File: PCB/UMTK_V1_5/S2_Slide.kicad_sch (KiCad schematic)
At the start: 6 parts, among them J6 JST 4pin, J7 47589-0001, J8 10033526-N3212LF

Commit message: Updating Schematic
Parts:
- added U11, U12: SN74LVC1T45DCK, Package_TO_SOT_SMD:SOT-363_SC-70-6, symbol Logic_LevelTranslator:SN74LVC1T45DCK
- JP1: value Slide_DAT_Swap -> SLIDE_DAT_DIR
- JP2: value Slide_CLK_Swap -> SLIDE_CLK_DIR
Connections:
- net +5V: now also U11.6 (VCCB), U12.6 (VCCB)
- net GND: now also JP1.3 (B), JP2.1 (A), U11.2 (GND), U12.2 (GND)
- net SLIDE_CLK: now also U11.3 (A); no longer J6.3, J7.3 (D+), J8.3 (D+), JP1.3 (B), JP2.1 (A), JP2.2 (C)
- net SLIDE_DAT: now also U12.3 (A); no longer J6.2, J7.2 (D-), J8.2 (D-), JP1.1 (A), JP1.2 (C), JP2.3 (B)
- new net: JP2.2 (C), U12.5 (DIR)
- new net: JP1.2 (C), U11.5 (DIR)
- new net VDD: JP1.1 (A), JP2.3 (B), U11.1 (VCCA), U12.1 (VCCA)
- new net _SLIDE_CLK: J6.3, J7.3 (D+), J8.3 (D+), U11.4 (B), U12.4 (B)
- new net _SLIDE_DAT_: J6.2, J7.2 (D-), J8.2 (D-)
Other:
- moved on the sheet: J6, J7, J8, JP3

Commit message: Schematic Done, Assigning footprint
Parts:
- removed JP1: SLIDE_DAT_DIR, symbol Jumper:Jumper_3_Bridged12
- removed JP2: SLIDE_CLK_DIR, symbol Jumper:Jumper_3_Bridged12
- renumbered JP3 to JP2
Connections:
- net SLIDE_DAT_DIR: now reaches U12.5 (DIR)
- net SLIDE_CLK_DIR: now reaches U11.5 (DIR)

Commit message: Footprint assign
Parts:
- J6: footprint 4Pin JST -> Connector_JST:JST_XH_B2B-XH-AM_1x02_P2.50mm_Vertical
- J7: footprint MOLX-47589-0001_V -> digikey-footprints:USB_Micro_AB_Female_0475890001
- J8: footprint FCI-10033526-N3212LF_V -> digikey-footprints:USB_Mini_B_Female_548190519
- JP2: footprint (none) -> Jumper:SolderJumper-3_P1.3mm_Bridged12_Pad1.0x1.5mm
- U11, U12: footprint Package_TO_SOT_SMD:SOT-363_SC-70-6 -> Package_TO_SOT_SMD:SOT-23-6
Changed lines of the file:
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@@
 			)
 		)
-		(property "Footprint" "4Pin JST"
+		(property "Footprint" "Connector_JST:JST_XH_B2B-XH-AM_1x02_P2.50mm_Vertical"
 			(at 152.4 105.41 0)
 			(effects
@@
 			)
 		)
-		(property "Footprint" "FCI-10033526-N3212LF_V"
+		(property "Footprint" "digikey-footprints:USB_Mini_B_Female_548190519"
 			(at 210.82 88.9 0)
 			(effects
@@
 			)
 		)
-		(property "Footprint" ""
+		(property "Footprint" "Jumper:SolderJumper-3_P1.3mm_Bridged12_Pad1.0x1.5mm"
 			(at 118.11 91.44 0)
 			(effects
@@
 			)
 		)
-		(property "Footprint" "MOLX-47589-0001_V"
+		(property "Footprint" "digikey-footprints:USB_Micro_AB_Female_0475890001"
 			(at 175.26 88.9 0)
 			(effects
@@
 			)
 		)
-		(property "Footprint" "Package_TO_SOT_SMD:SOT-363_SC-70-6"
+		(property "Footprint" "Package_TO_SOT_SMD:SOT-23-6"
 			(at 64.77 95.25 0)
 			(effects
@@
 			)
 		)
-		(property "Footprint" "Package_TO_SOT_SMD:SOT-363_SC-70-6"
+		(property "Footprint" "Package_TO_SOT_SMD:SOT-23-6"
 			(at 64.77 140.97 0)
 			(effects

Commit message: ERC good, imported into PCB
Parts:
- J6: footprint Connector_JST:JST_XH_B2B-XH-AM_1x02_P2.50mm_Vertical -> Connector_JST:JST_XH_B4B-XH-A_1x04_P2.50mm_Vertical
- U11, U12: footprint Package_TO_SOT_SMD:SOT-23-6 -> Package_TO_SOT_SMD:SOT-363_SC-70-6
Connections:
- no-connect marks 0 -> 2
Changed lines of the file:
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@@
 		(color 0 0 0 0)
+	)
+	(no_connect
+		(at 205.74 99.06)
+	)
+	(no_connect
+		(at 170.18 99.06)
 	)
 	(wire
@@
 			)
 		)
-		(property "Description" ""
+		(property "Description" "Power symbol creates a global label with name \"+5V\""
 			(at 111.76 86.36 0)
 			(effects
@@
 			)
 		)
-		(property "Description" ""
+		(property "Description" "Power symbol creates a global label with name 'GND'"
 			(at 170.18 119.38 0)
 			(effects
@@
 			)
 		)
-		(property "Footprint" "Connector_JST:JST_XH_B2B-XH-AM_1x02_P2.50mm_Vertical"
+		(property "Footprint" "Connector_JST:JST_XH_B4B-XH-A_1x04_P2.50mm_Vertical"
 			(at 152.4 105.41 0)
 			(effects
@@
 			)
 		)
-		(property "Description" ""
+		(property "Description" "Mini USB B-Type, 5-Pin SMD, RoHS, Tape and Reel"
 			(at 210.82 88.9 0)
 			(effects
@@
 			)
 		)
-		(property "Description" ""
+		(property "Description" "Jumper, 3-pole, pins 1+2 closed/bridged"
 			(at 118.11 91.44 0)
 			(effects
@@
 			)
 		)
-		(property "Description" ""
+		(property "Description" "Right Angle Female Type AB Micro USB Connector, 30 V, 1.8 A, -30 to 85 degC, RoHS, Tape and Reel"
 			(at 175.26 88.9 0)
 			(effects
@@
 			)
 		)
-		(property "Description" ""
+		(property "Description" "Power symbol creates a global label with name 'GND'"
 			(at 144.78 115.57 0)
 			(effects
@@
 			)
 		)
-		(property "Description" ""
+		(property "Description" "Power symbol creates a global label with name \"+3V3\""
 			(at 109.22 97.79 0)
 			(effects
@@
 			)
 		)
-		(property "Footprint" "Package_TO_SOT_SMD:SOT-23-6"
+		(property "Footprint" "Package_TO_SOT_SMD:SOT-363_SC-70-6"
 			(at 64.77 95.25 0)
 			(effects
@@
 			)
 		)
-		(property "Footprint" "Package_TO_SOT_SMD:SOT-23-6"
+		(property "Footprint" "Package_TO_SOT_SMD:SOT-363_SC-70-6"
 			(at 64.77 140.97 0)
 			(effects
@@
 			)
 		)
-		(property "Description" ""
+		(property "Description" "Power symbol creates a global label with name 'GND'"
 			(at 205.74 119.38 0)
 			(effects

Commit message: Initial Place, Board Stack
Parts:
- removed J6: JST 4pin, Connector_JST:JST_XH_B4B-XH-A_1x04_P2.50mm_Vertical, symbol UMTK-altium-import:0_4Pin JST
- removed J7: 47589-0001, digikey-footprints:USB_Micro_AB_Female_0475890001, symbol UMTK-altium-import:0_USB-5-6SHLD
- added JP3: Slide Logic LVL, Jumper:SolderJumper-3_P1.3mm_Bridged12_Pad1.0x1.5mm, symbol Jumper:Jumper_3_Bridged12
- J8: footprint digikey-footprints:USB_Mini_B_Female_548190519 -> Connector_USB:USB_Mini-B_Wuerth_65100516121_Horizontal
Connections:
- net +3V3: now also JP3.1 (A)
- net +5V: now also JP3.3 (B); no longer U11.6 (VCCB), U12.6 (VCCB)
- net _SLIDE_DAT_: now also U12.4 (B)
- net _SLIDE_CLK renamed _SLIDE_CLK_
- net _SLIDE_CLK_: no longer U12.4 (B)
- new net _SLIDE_DATA_LVL_: JP3.2 (C), U11.6 (VCCB), U12.6 (VCCB)
- no-connect marks 2 -> 1
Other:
- moved on the sheet: J8

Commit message: Layout Started
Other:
- moved on the sheet: J8
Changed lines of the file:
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@@
 	(paper "A4")
 	(junction
-		(at 154.94 109.22)
+		(at 184.15 114.3)
 		(diameter 0)
 		(color 0 0 0 0)
 	)
 	(junction
-		(at 154.94 111.76)
+		(at 184.15 116.84)
 		(diameter 0)
 		(color 0 0 0 0)
 	)
 	(junction
-		(at 154.94 114.3)
+		(at 184.15 119.38)
 		(diameter 0)
 		(color 0 0 0 0)
 	)
 	(junction
-		(at 154.94 116.84)
+		(at 184.15 121.92)
 		(diameter 0)
 		(color 0 0 0 0)
 	)
 	(no_connect
-		(at 154.94 104.14)
+		(at 184.15 109.22)
 	)
 	(wire
@@
 	(wire
 		(pts
+			(xy 147.32 101.6) (xy 184.15 101.6)
+		)
+		(stroke
+			(width 0)
+			(type default)
+		)
+	)
+	(wire
+		(pts
 			(xy 107.95 121.92) (xy 110.49 121.92)
 		)
@@
 	(wire
 		(pts
-			(xy 154.94 124.46) (xy 154.94 116.84)
+			(xy 184.15 129.54) (xy 184.15 121.92)
 		)
 		(stroke
@@
 	(wire
 		(pts
-			(xy 154.94 114.3) (xy 154.94 111.76)
+			(xy 147.32 91.44) (xy 147.32 101.6)
+		)
+		(stroke
+			(width 0)
+			(type default)
+		)
+	)
+	(wire
+		(pts
+			(xy 184.15 119.38) (xy 184.15 116.84)
 		)
 		(stroke
@@
 	(wire
 		(pts
-			(xy 152.4 99.06) (xy 154.94 99.06)
+			(xy 181.61 104.14) (xy 184.15 104.14)
 		)
 		(stroke
@@
 	(wire
 		(pts
-			(xy 154.94 111.76) (xy 154.94 109.22)
+			(xy 184.15 116.84) (xy 184.15 114.3)
 		)
 		(stroke
@@
 	(wire
 		(pts
-			(xy 151.13 91.44) (xy 121.92 91.44)
-		)
-		(stroke
-			(width 0)
-			(type default)
-		)
-	)
-	(wire
-		(pts
 			(xy 110.49 121.92) (xy 110.49 120.65)
 		)
@@
 	(wire
 		(pts
-			(xy 151.13 96.52) (xy 151.13 91.44)
-		)
-		(stroke
-			(width 0)
-			(type default)
-		)
-	)
-	(wire
-		(pts
-			(xy 152.4 101.6) (xy 154.94 101.6)
-		)
-		(stroke
-			(width 0)
-			(type default)
-		)
-	)
-	(wire
-		(pts
-			(xy 151.13 96.52) (xy 154.94 96.52)
+			(xy 181.61 106.68) (xy 184.15 106.68)
+		)
+		(stroke
+			(width 0)
+			(type default)
+		)
+	)
+	(wire
+		(pts
+			(xy 121.92 91.44) (xy 147.32 91.44)
 		)
 		(stroke
@@
 	(wire
 		(pts
-			(xy 154.94 109.22) (xy 154.94 106.68)
+			(xy 184.15 114.3) (xy 184.15 111.76)
 		)
 		(stroke
@@
 	(wire
 		(pts
-			(xy 154.94 116.84) (xy 154.94 114.3)
+			(xy 184.15 121.92) (xy 184.15 119.38)
 		)
 		(stroke
@@
 	)
 	(label "_SLIDE_DAT_"
-		(at 152.4 99.06 180)
+		(at 181.61 104.14 180)
 		(fields_autoplaced yes)
 		(effects
@@
 	)
 	(label "_SLIDE_CLK_"
-		(at 152.4 101.6 180)
+		(at 181.61 106.68 180)
 		(fields_autoplaced yes)
 		(effects
@@
 	(symbol
 		(lib_id "UMTK-altium-import:0_USB-5-4SHLD")
-		(at 160.02 93.98 0)
+		(at 189.23 99.06 0)
 		(unit 1)
 		(exclude_from_sim no)
@@
 		(dnp no)
 		(property "Reference" "J8"
-			(at 159.766 93.726 0)
+			(at 188.976 98.806 0)
 			(effects
 				(font
@@
 		)
 		(property "Value" "10033526-N3212LF"
-			(at 159.766 122.174 0)
+			(at 188.976 127.254 0)
 			(effects
 				(font
@@
 		)
 		(property "Footprint" "Connector_USB:USB_Mini-B_Wuerth_65100516121_Horizontal"
-			(at 160.02 93.98 0)
+			(at 189.23 99.06 0)
 			(effects
 				(font
@@
 		)
 		(property "Datasheet" ""
-			(at 160.02 93.98 0)
+			(at 189.23 99.06 0)
 			(effects
 				(font
@@
 		)
 		(property "Description" "Mini USB B-Type, 5-Pin SMD, RoHS, Tape and Reel"
-			(at 160.02 93.98 0)
+			(at 189.23 99.06 0)
 			(effects
 				(font
@@
 		)
 		(property "PARTNUMBER" "10033526-N3212LF"
-			(at 154.432 90.17 0)
+			(at 183.642 95.25 0)
 			(effects
 				(font
@@
 		)
 		(property "DATASHEETVERSION" "Rev. N"
-			(at 154.432 90.17 0)
+			(at 183.642 95.25 0)
 			(effects
 				(font
@@
 		)
 		(property "TERMINATION STYLE" "Solder Pad"
-			(at 154.432 90.17 0)
+			(at 183.642 95.25 0)
 			(effects
 				(font
@@
 		)
 		(property "PACKAGING" "Reel"
-			(at 154.432 90.17 0)
+			(at 183.642 95.25 0)
 			(effects
 				(font
@@
 		)
 		(property "SHELL PLATING" "Nickel"
-			(at 154.432 90.17 0)
+			(at 183.642 95.25 0)
 			(effects
 				(font
@@
 		)
 		(property "STANDARD" "USB"
-			(at 154.432 90.17 0)
+			(at 183.642 95.25 0)
 			(effects
 				(font
@@
 		)
 		(property "COLOR" "Black"
-			(at 154.432 90.17 0)
+			(at 183.642 95.25 0)
 			(effects
 				(font
@@
 		)
 		(property "COMPONENTLINK1DESCRIPTION" "Manufacturer URL"
-			(at 154.432 90.17 0)
+			(at 183.642 95.25 0)
 			(effects
 				(font
@@
 		)
 		(property "MOUNTING TECHNOLOGY" "Surface Mount"
-			(at 154.432 90.17 0)
+			(at 183.642 95.25 0)
 			(effects
 				(font
@@
 		)
 		(property "FACTORY PACK QUANTITY" "750"
-			(at 154.432 90.17 0)
+			(at 183.642 95.25 0)
 			(effects
 				(font
@@
 		)
 		(property "MOUNTING ANGLE" "Right"
-			(at 154.432 90.17 0)
+			(at 183.642 95.25 0)
 			(effects
 				(font
@@
 		)
 		(property "CONTACT MATERIAL" "Copper Alloy"
-			(at 154.432 90.17 0)
+			(at 183.642 95.25 0)
 			(effects
 				(font
@@
 		)
 		(property "NUMBER OF PORTS" "1 Port"
-			(at 154.432 90.17 0)
+			(at 183.642 95.25 0)
 			(effects
 				(font
@@
 		)
 		(property "PRODUCT CATEGORY" "USB Connectors"
-			(at 154.432 90.17 0)
+			(at 183.642 95.25 0)
 			(effects
 				(font
@@
 		)
 		(property "MANUFACTURER" "FCI"
-			(at 154.432 90.17 0)
+			(at 183.642 95.25 0)
 			(effects
 				(font
@@
 		)
 		(property "COMPONENTLINK2URL" "http://portal.fciconnect.com/Comergent//fci/drawing/10033526.pdf"
-			(at 154.432 90.17 0)
+			(at 183.642 95.25 0)
 			(effects
 				(font
@@
 		)
 		(property "FLAMMABILITY RATING" "UL 94 V-0"
-			(at 154.432 90.17 0)
+			(at 183.642 95.25 0)
 			(effects
 				(font
@@
 		)
 		(property "PRODUCT" "Mini USB Type B Connectors"
-			(at 154.432 90.17 0)
+			(at 183.642 95.25 0)
 			(effects
 				(font
@@
 		)
 		(property "CONTACT PLATING" "Gold"
-			(at 154.432 90.17 0)
+			(at 183.642 95.25 0)
 			(effects
 				(font
@@
 		)
 		(property "COMPONENTLINK2DESCRIPTION" "Datasheet"
-			(at 154.432 90.17 0)
+			(at 183.642 95.25 0)
 			(effects
 				(font
@@
 		)
 		(property "BRAND" "FCI"
-			(at 154.432 90.17 0)
+			(at 183.642 95.25 0)
 			(effects
 				(font
@@
 		)
 		(property "NUMBER OF CONTACTS" "5 Contact"
-			(at 154.432 90.17 0)
+			(at 183.642 95.25 0)
 			(effects
 				(font
@@
 		)
 		(property "ROHS" "Details"
-			(at 154.432 90.17 0)
+			(at 183.642 95.25 0)
 			(effects
 				(font
@@
 		)
 		(property "CONNECTOR TYPE" "Mini USB Type B Receptacle"
-			(at 154.432 90.17 0)
+			(at 183.642 95.25 0)
 			(effects
 				(font
@@
 		)
 		(property "COMPONENTLINK1URL" "http://portal.fciconnect.com/"
-			(at 154.432 90.17 0)
+			(at 183.642 95.25 0)
 			(effects
 				(font
@@
 		)
 		(property "GENDER" "Female"
-			(at 154.432 90.17 0)
+			(at 183.642 95.25 0)
 			(effects
 				(font
@@
 		)
 		(property "INSULATION RESISTANCE" "100 MOhms"
-			(at 154.432 90.17 0)
+			(at 183.642 95.25 0)
 			(effects
 				(font
@@
 		)
 		(property "PACKAGEDESCRIPTION" "5-Pin Surface Mount Device, Body 9.2 x 7.7 mm, Pitch 0.8 mm"
-			(at 154.432 90.17 0)
+			(at 183.642 95.25 0)
 			(effects
 				(font
@@
 	(symbol
 		(lib_id "UMTK-altium-import:GND")
-		(at 154.94 124.46 0)
+		(at 184.15 129.54 0)
 		(unit 1)
 		(exclude_from_sim no)
@@
 		(dnp no)
 		(property "Reference" "#PWR070"
-			(at 154.94 124.46 0)
+			(at 184.15 129.54 0)
 			(effects
 				(font
@@
 		)
 		(property "Value" "GND"
-			(at 154.94 130.81 0)
+			(at 184.15 135.89 0)
 			(effects
 				(font
@@
 		)
 		(property "Footprint" ""
-			(at 154.94 124.46 0)
+			(at 184.15 129.54 0)
 			(effects
 				(font
@@
 		)
 		(property "Datasheet" ""
-			(at 154.94 124.46 0)
+			(at 184.15 129.54 0)
 			(effects
 				(font
@@
 		)
 		(property "Description" "Power symbol creates a global label with name 'GND'"
-			(at 154.94 124.46 0)
-			(effects
-				(font
+			(at 184.15 129.54 0)
+			(effects
+				(font

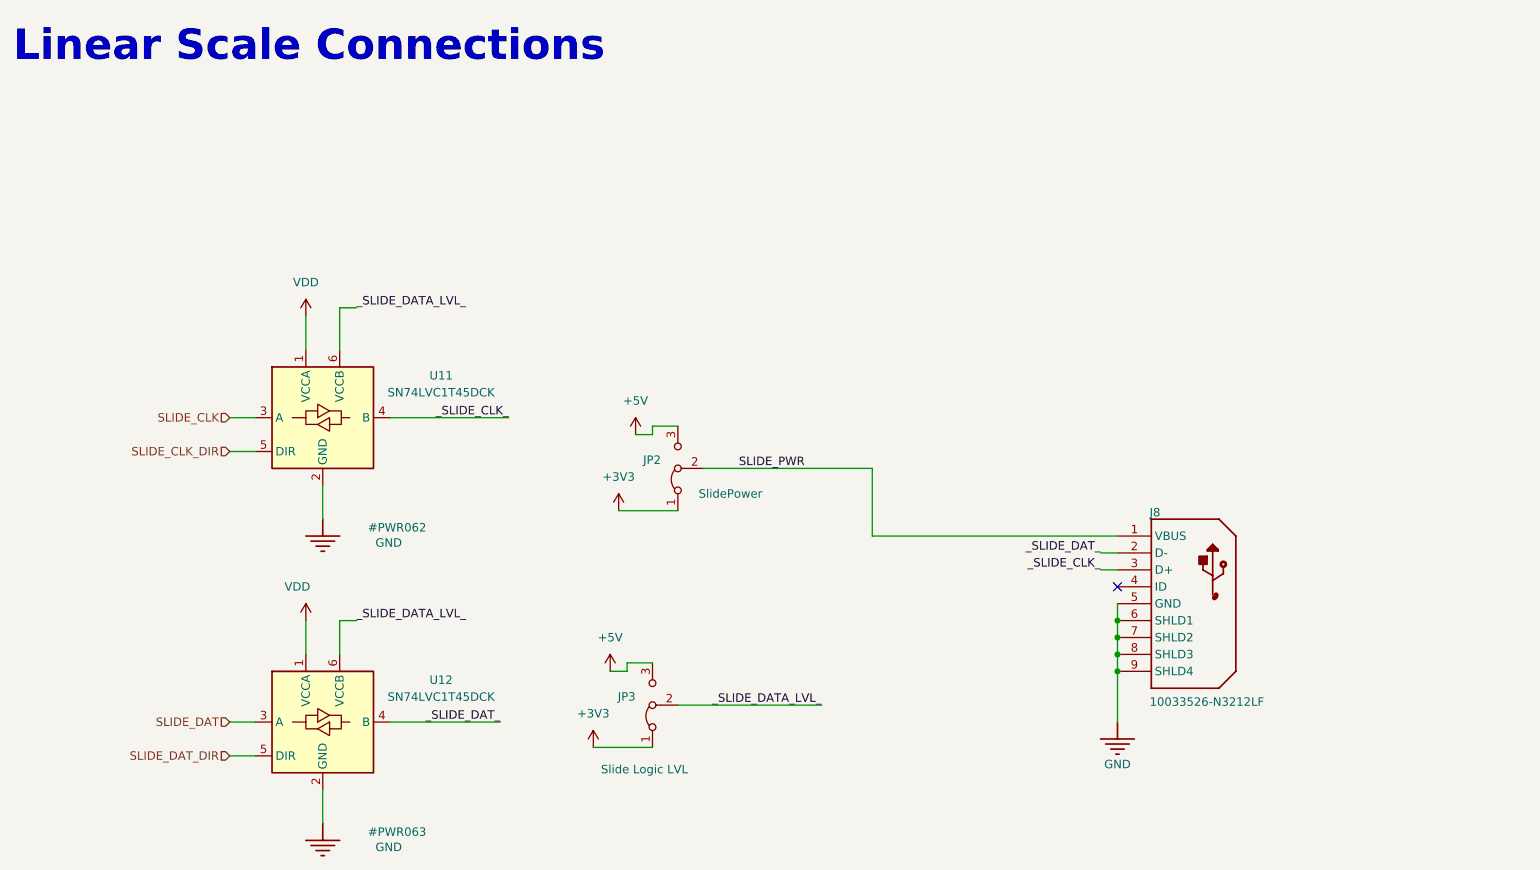
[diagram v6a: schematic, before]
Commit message: Updated slide pinout, add protection, Fixed some issues
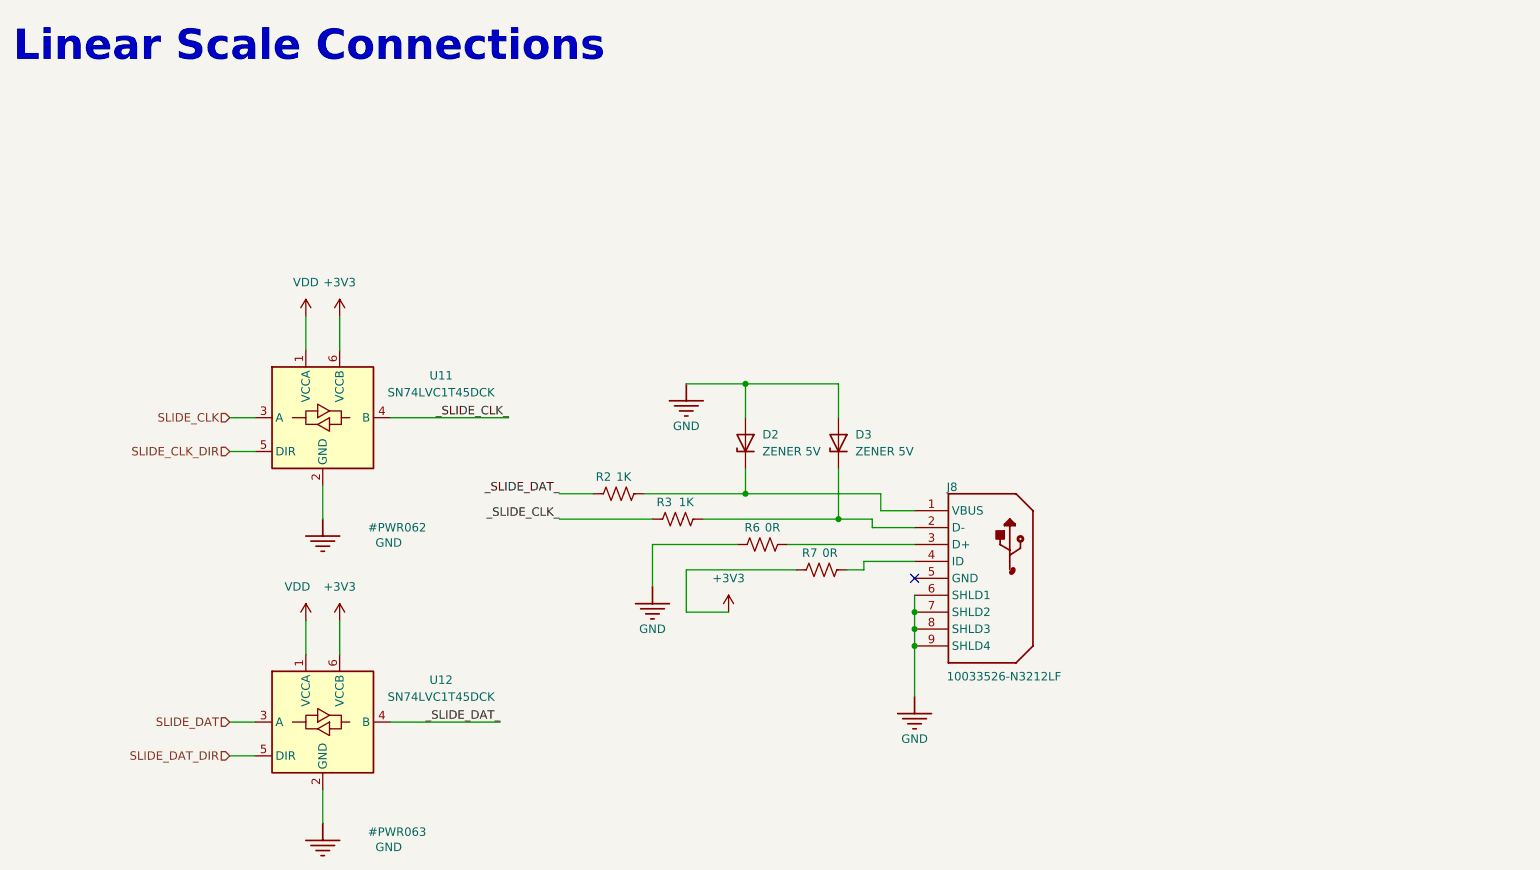
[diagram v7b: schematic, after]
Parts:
- removed JP2: SlidePower, Jumper:SolderJumper-3_P1.3mm_Bridged12_Pad1.0x1.5mm, symbol Jumper:Jumper_3_Bridged12
- removed JP3: Slide Logic LVL, Jumper:SolderJumper-3_P1.3mm_Bridged12_Pad1.0x1.5mm, symbol Jumper:Jumper_3_Bridged12
- added D2, D3: ZENER 5V, Diode_SMD:D_SOD-523, symbol Diode:ESD5Zxx
- added R2, R3: 1K, Resistor_SMD:R_0603_1608Metric, symbol Device:R_US
- added R6, R7: 0R, Resistor_SMD:R_0603_1608Metric, symbol Device:R_US
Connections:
- net _SLIDE_DATA_LVL_ is gone; now on net +3V3: U11.6 (VCCB), U12.6 (VCCB)
- net +3V3: now also R7.1
- net GND: now also D2.2 (A), D3.2 (A), R6.1; no longer J8.5 (GND)
- net _SLIDE_CLK_: now also R3.1; no longer J8.3 (D+)
- net _SLIDE_DAT_: now also R2.1; no longer J8.2 (D-)
- net at J8.4 (ID): now also R7.2
- net SLIDE_PWR: no longer names the net of J8.1 (VBUS)
- net SLIDE_PWR: now also D2.1 (K), R2.2
- new net: J8.3 (D+), R6.2
- new net: D3.1 (K), J8.2 (D-), R3.2
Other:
- moved on the sheet: J8
